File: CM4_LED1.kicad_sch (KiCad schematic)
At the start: 3 parts

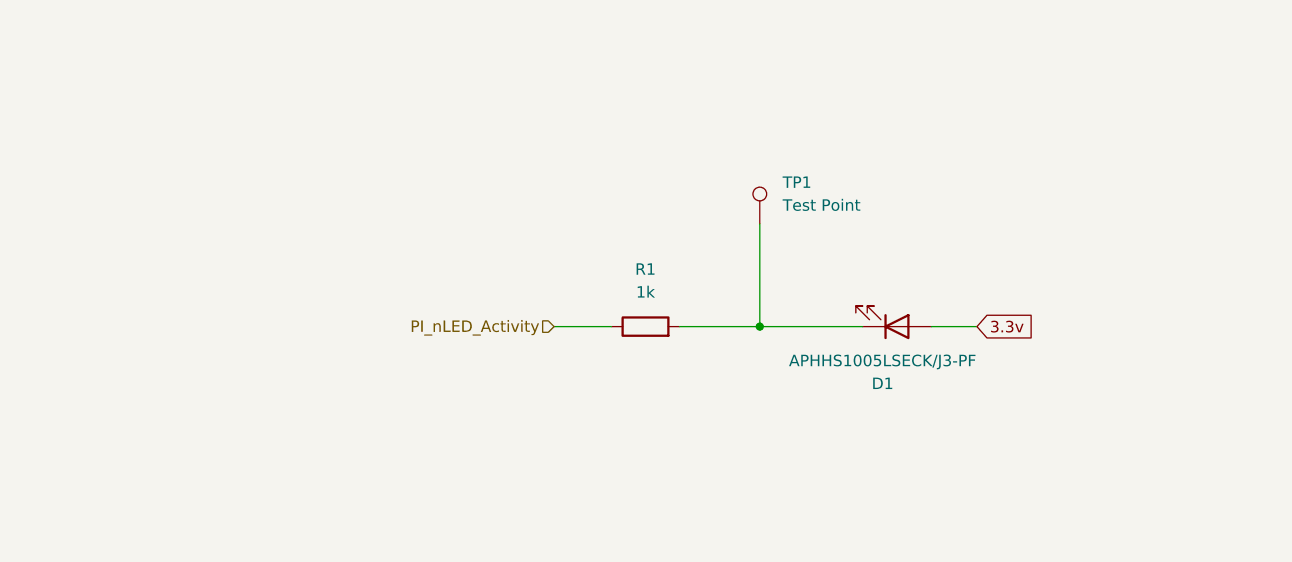
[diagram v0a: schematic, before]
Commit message: added gitignore, and did work on CM4
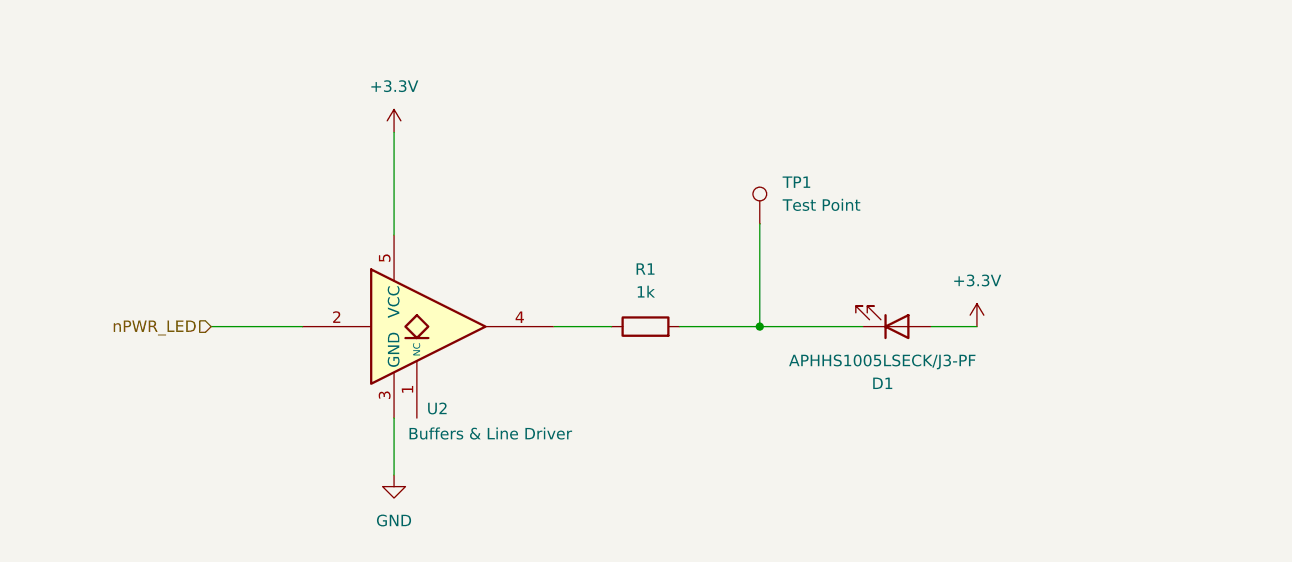
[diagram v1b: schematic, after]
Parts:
- added U2: Buffers & Line Driver, dz_dio:SOT65P210X110-5N, symbol #dzdb:s_misc/D-DIO-74LVC1G07SE-7
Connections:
- net 3.3v renamed +3.3V
- net +3.3V: now also U2.5 (VCC)
- net PI_nLED_Activity: no longer names the net of R1.1
- net PI_nLED_Activity: now also U2.4
- new net GND: U2.3 (GND)
- new net nPWR_LED: U2.2

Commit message: Added other LED indicators, ethernet and connector (main connector to other pcb's)
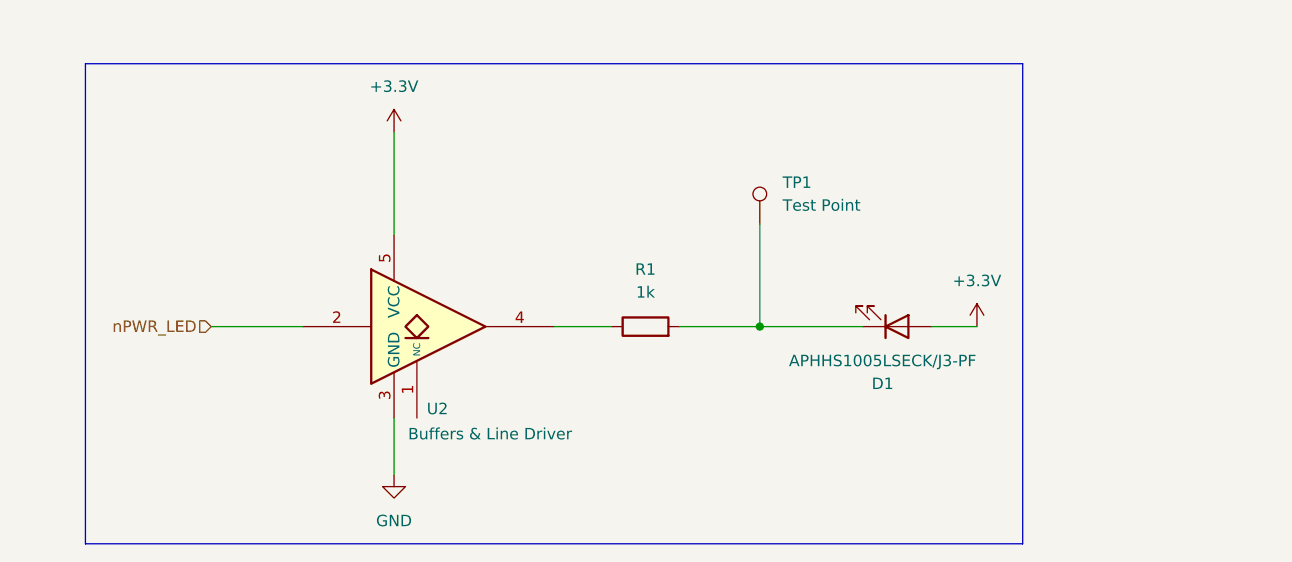
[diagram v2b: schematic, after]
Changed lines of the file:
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@@
 	(generator_version "9.0")
 	(paper "A4")
+	(rectangle
+		(start 71.12 45.72)
+		(end 175.26 99.06)
+		(stroke
+			(width 0)
+			(type default)
+		)
+		(fill
+			(type none)
+		)
+	)
 	(junction
 		(at 146.05 74.93)

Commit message: minor changes/cleanup
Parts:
- renumbered D1 to D2, R1 to R2, TP1 to TP2, U2 to U1
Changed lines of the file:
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@@
 		(on_board yes)
 		(dnp no)
-		(property "Reference" "D1"
+		(property "Reference" "D2"
 			(at 159.7025 81.28 0)
 			(effects
@@
 		(instances
 			(project "nautilus_mainboard"
-				(path "/ce1819b2-f280-40ed-834f-6fe4d12f809d/c2b6dac3-d6fd-4d5d-bd17-0cff91db88eb/b11889ff-9e53-460e-a5df-2ddc3c461adc/3057b5eb-f1b7-4f0b-8332-d97cb83907a8/e0935ee6-fc77-4de6-a0ac-caf50bea3bcd"
-					(reference "D1")
+				(path "/ce1819b2-f280-40ed-834f-6fe4d12f809d/c2b6dac3-d6fd-4d5d-bd17-0cff91db88eb/0837dad1-ec16-488a-a684-981e55247089/e0935ee6-fc77-4de6-a0ac-caf50bea3bcd"
+					(reference "D2")
 					(unit 1)
 				)
@@
 		(dnp no)
 		(fields_autoplaced yes)
-		(property "Reference" "#PWR08"
+		(property "Reference" "#PWR011"
 			(at 105.41 97.79 0)
 			(effects
@@
 		)
 		(instances
-			(project ""
-				(path "/ce1819b2-f280-40ed-834f-6fe4d12f809d/c2b6dac3-d6fd-4d5d-bd17-0cff91db88eb/b11889ff-9e53-460e-a5df-2ddc3c461adc/3057b5eb-f1b7-4f0b-8332-d97cb83907a8/e0935ee6-fc77-4de6-a0ac-caf50bea3bcd"
-					(reference "#PWR08")
+			(project "nautilus_mainboard"
+				(path "/ce1819b2-f280-40ed-834f-6fe4d12f809d/c2b6dac3-d6fd-4d5d-bd17-0cff91db88eb/0837dad1-ec16-488a-a684-981e55247089/e0935ee6-fc77-4de6-a0ac-caf50bea3bcd"
+					(reference "#PWR011")
 					(unit 1)
 				)
@@
 		(on_board yes)
 		(dnp no)
-		(property "Reference" "U2"
+		(property "Reference" "U1"
 			(at 110.236 84.074 0)
 			(effects
@@
 		)
 		(instances
-			(project ""
-				(path "/ce1819b2-f280-40ed-834f-6fe4d12f809d/c2b6dac3-d6fd-4d5d-bd17-0cff91db88eb/b11889ff-9e53-460e-a5df-2ddc3c461adc/3057b5eb-f1b7-4f0b-8332-d97cb83907a8/e0935ee6-fc77-4de6-a0ac-caf50bea3bcd"
-					(reference "U2")
+			(project "nautilus_mainboard"
+				(path "/ce1819b2-f280-40ed-834f-6fe4d12f809d/c2b6dac3-d6fd-4d5d-bd17-0cff91db88eb/0837dad1-ec16-488a-a684-981e55247089/e0935ee6-fc77-4de6-a0ac-caf50bea3bcd"
+					(reference "U1")
 					(unit 1)
 				)
@@
 		(dnp no)
 		(fields_autoplaced yes)
-		(property "Reference" "#PWR07"
+		(property "Reference" "#PWR012"
 			(at 170.18 78.74 0)
 			(effects
@@
 		)
 		(instances
-			(project ""
-				(path "/ce1819b2-f280-40ed-834f-6fe4d12f809d/c2b6dac3-d6fd-4d5d-bd17-0cff91db88eb/b11889ff-9e53-460e-a5df-2ddc3c461adc/3057b5eb-f1b7-4f0b-8332-d97cb83907a8/e0935ee6-fc77-4de6-a0ac-caf50bea3bcd"
-					(reference "#PWR07")
+			(project "nautilus_mainboard"
+				(path "/ce1819b2-f280-40ed-834f-6fe4d12f809d/c2b6dac3-d6fd-4d5d-bd17-0cff91db88eb/0837dad1-ec16-488a-a684-981e55247089/e0935ee6-fc77-4de6-a0ac-caf50bea3bcd"
+					(reference "#PWR012")
 					(unit 1)
 				)
@@
 		(dnp no)
 		(fields_autoplaced yes)
-		(property "Reference" "R1"
+		(property "Reference" "R2"
 			(at 133.35 68.58 90)
 			(effects
@@
 		(instances
 			(project "nautilus_mainboard"
-				(path "/ce1819b2-f280-40ed-834f-6fe4d12f809d/c2b6dac3-d6fd-4d5d-bd17-0cff91db88eb/b11889ff-9e53-460e-a5df-2ddc3c461adc/3057b5eb-f1b7-4f0b-8332-d97cb83907a8/e0935ee6-fc77-4de6-a0ac-caf50bea3bcd"
-					(reference "R1")
+				(path "/ce1819b2-f280-40ed-834f-6fe4d12f809d/c2b6dac3-d6fd-4d5d-bd17-0cff91db88eb/0837dad1-ec16-488a-a684-981e55247089/e0935ee6-fc77-4de6-a0ac-caf50bea3bcd"
+					(reference "R2")
 					(unit 1)
 				)
@@
 		(dnp no)
 		(fields_autoplaced yes)
-		(property "Reference" "#PWR09"
+		(property "Reference" "#PWR010"
 			(at 105.41 57.15 0)
 			(effects
@@
 		(instances
 			(project "nautilus_mainboard"
-				(path "/ce1819b2-f280-40ed-834f-6fe4d12f809d/c2b6dac3-d6fd-4d5d-bd17-0cff91db88eb/b11889ff-9e53-460e-a5df-2ddc3c461adc/3057b5eb-f1b7-4f0b-8332-d97cb83907a8/e0935ee6-fc77-4de6-a0ac-caf50bea3bcd"
-					(reference "#PWR09")
+				(path "/ce1819b2-f280-40ed-834f-6fe4d12f809d/c2b6dac3-d6fd-4d5d-bd17-0cff91db88eb/0837dad1-ec16-488a-a684-981e55247089/e0935ee6-fc77-4de6-a0ac-caf50bea3bcd"
+					(reference "#PWR010")
 					(unit 1)
 				)
@@
 		(dnp no)
 		(fields_autoplaced yes)
-		(property "Reference" "TP1"
+		(property "Reference" "TP2"
 			(at 148.59 58.9279 0)
 			(effects
@@
 		(instances
 			(project "nautilus_mainboard"
-				(path "/ce1819b2-f280-40ed-834f-6fe4d12f809d/c2b6dac3-d6fd-4d5d-bd17-0cff91db88eb/b11889ff-9e53-460e-a5df-2ddc3c461adc/3057b5eb-f1b7-4f0b-8332-d97cb83907a8/e0935ee6-fc77-4de6-a0ac-caf50bea3bcd"
-					(reference "TP1")
+				(path "/ce1819b2-f280-40ed-834f-6fe4d12f809d/c2b6dac3-d6fd-4d5d-bd17-0cff91db88eb/0837dad1-ec16-488a-a684-981e55247089/e0935ee6-fc77-4de6-a0ac-caf50bea3bcd"
+					(reference "TP2")
 					(unit 1)
 				)

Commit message: simple changes
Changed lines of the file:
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@@
 	(generator_version "9.0")
 	(paper "A4")
-	(rectangle
-		(start 71.12 45.72)
-		(end 175.26 99.06)
+	(text_box "Directly copied from the official CM4 io board (indicator LED for 3.3v)"
+		(exclude_from_sim no)
+		(at 66.04 40.64 0)
+		(size 111.76 58.42)
+		(margins 0.9525 0.9525 0.9525 0.9525)
 		(stroke
 			(width 0)
-			(type default)
+			(type solid)
 		)
 		(fill
 			(type none)
 		)
+		(effects
+			(font
+				(size 1.27 1.27)
+			)
+			(justify left top)
+		)
 	)

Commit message: Added Power logic finally. (plus some comments on further improvements)
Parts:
- renumbered D2 to D1, R2 to R5, TP2 to TP1
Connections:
- net +3.3V renamed Battery_Out_3.3V
- net Battery_Out_3.3V: no longer D1.2 (A)
- new net CM4_LED_IN_3.3V: D1.2 (A)
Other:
- note added: "<---"
- note added: "issue: will that logic work if I use USB vin only?"
- note added: "only use when connected completely? not over usb???"
- note added: "then I would in theory compare internal voltage with internal voltage... so probably not..."

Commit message: nearly complete with the PCB
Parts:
- renumbered U1 to U3
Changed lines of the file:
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@@
 		(on_board yes)
 		(dnp no)
-		(property "Reference" "U1"
+		(property "Reference" "U3"
 			(at 110.236 84.074 0)
 			(effects
@@
 			(project "nautilus_mainboard"
 				(path "/ce1819b2-f280-40ed-834f-6fe4d12f809d/c2b6dac3-d6fd-4d5d-bd17-0cff91db88eb/0837dad1-ec16-488a-a684-981e55247089/e0935ee6-fc77-4de6-a0ac-caf50bea3bcd"
-					(reference "U1")
+					(reference "U3")
 					(unit 1)
 				)

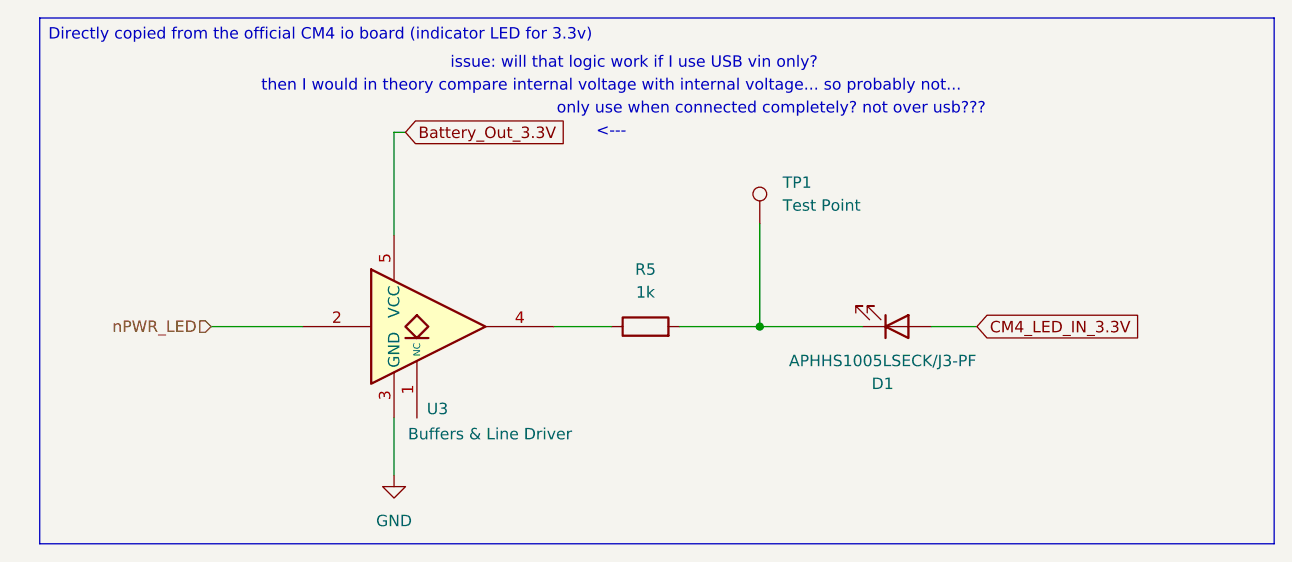
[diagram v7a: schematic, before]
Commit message: Symbal and naming changes
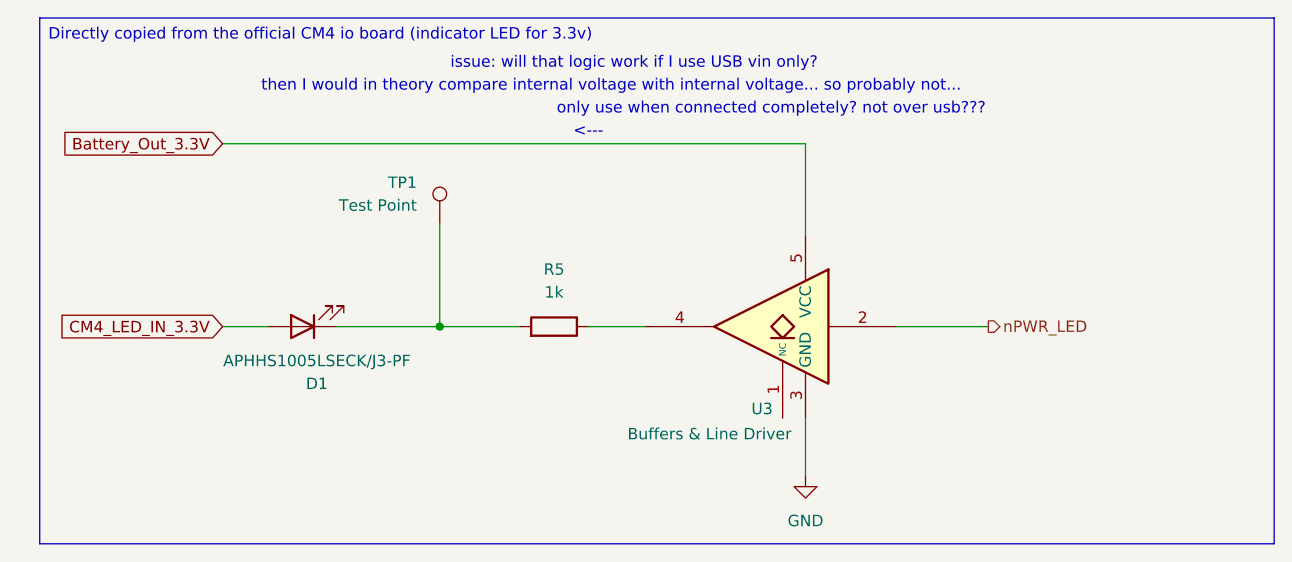
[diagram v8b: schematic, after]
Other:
- moved on the sheet: D1, R5, TP1, U3
